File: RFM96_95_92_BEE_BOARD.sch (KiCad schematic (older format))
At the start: 3 parts

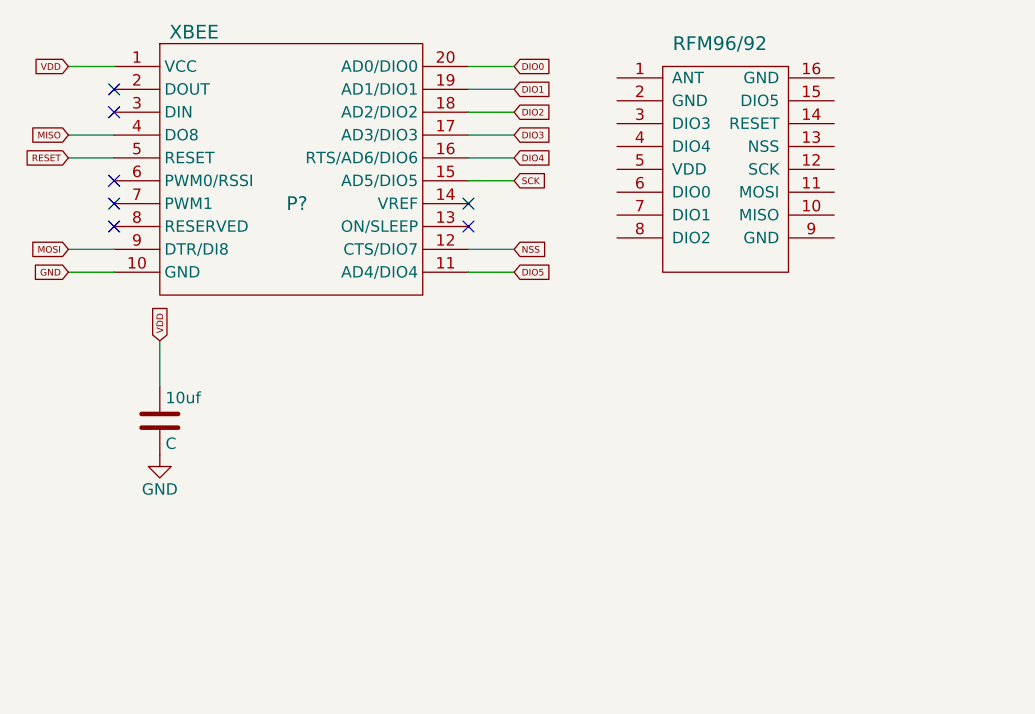
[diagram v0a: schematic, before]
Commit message: created library files and changed schematic
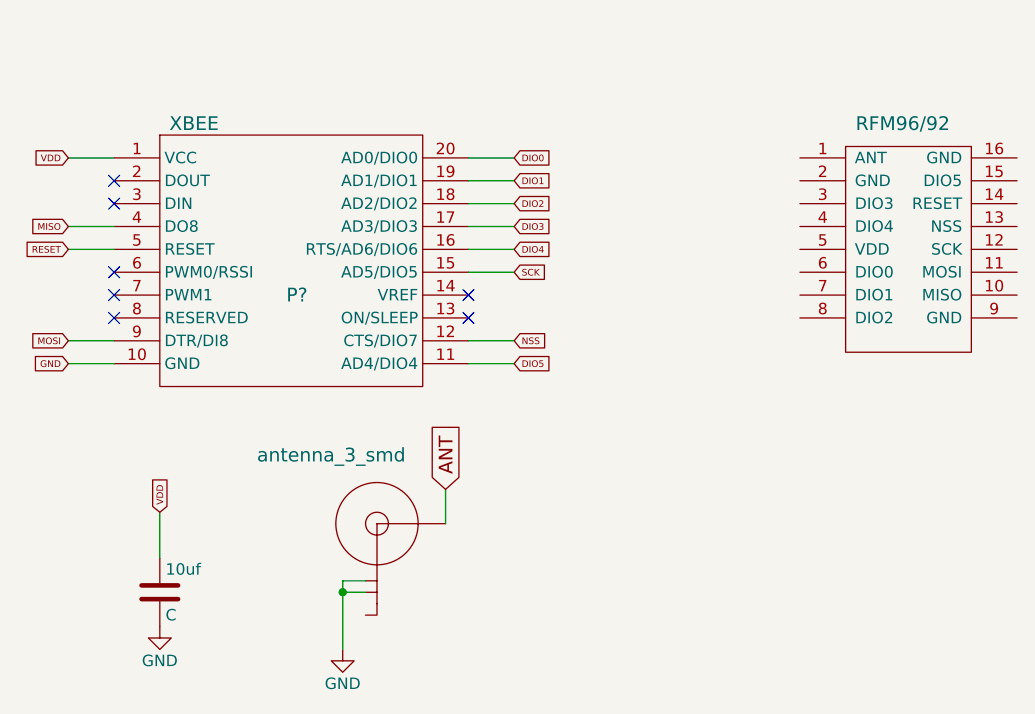
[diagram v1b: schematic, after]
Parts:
- added U?: antenna_3_smd, symbol antenna_3_smd
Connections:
- net labels added: ANT
- wire segments 14 -> 18
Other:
- moved on the sheet: 10uf, P?
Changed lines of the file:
@@
 LIBS:valves
 LIBS:RFM96_95_92
-LIBS:conn_8_16
-LIBS:conn_08_16
+LIBS:xbee
 LIBS:antenna
 LIBS:antenna_3_smd
-LIBS:conn_8_16_1
-LIBS:xbee
 LIBS:RFM96_95_92_BEE_BOARD-cache
 EELAYER 25 0
@@
 L RFM96/92 U?
 U 1 1 58359992
-P 5550 1600
-F 0 "U?" H 5600 1000 60  0001 C CNN
-F 1 "RFM96/92" H 5550 2150 60  0000 C CNN
-F 2 "" H 5750 1800 60  0001 C CNN
-F 3 "" H 5750 1800 60  0001 C CNN
-	1    5550 1600
+P 6350 1950
+F 0 "U?" H 6400 1350 60  0001 C CNN
+F 1 "RFM96/92" H 6350 2500 60  0000 C CNN
+F 2 "" H 6550 2150 60  0001 C CNN
+F 3 "" H 6550 2150 60  0001 C CNN
+	1    6350 1950
 	1    0    0    -1
 $EndComp
@@
 L XBEE P?
 U 1 1 583689AA
-P 3650 1700
-F 0 "P?" H 3700 1650 60  0000 C CNN
-F 1 "XBEE" H 3250 2400 60  0000 C CNN
-F 2 "" H 3650 1700 60  0001 C CNN
-F 3 "" H 3650 1700 60  0001 C CNN
-	1    3650 1700
+P 3650 2100
+F 0 "P?" H 3700 2050 60  0000 C CNN
+F 1 "XBEE" H 3250 2800 60  0000 C CNN
+F 2 "" H 3650 2100 60  0001 C CNN
+F 3 "" H 3650 2100 60  0001 C CNN
+	1    3650 2100
 	1    0    0    -1
 $EndComp
-NoConn ~ 4450 1750
-Text GLabel 2700 1150 0    29   Input ~ 0
+NoConn ~ 4450 2150
+Text GLabel 2700 1550 0    29   Input ~ 0
 VDD
-NoConn ~ 2900 1250
-NoConn ~ 2900 1350
-Text GLabel 2700 1450 0    29   Input ~ 0
-MISO
-Text GLabel 2700 1550 0    29   Input ~ 0
-RESET
 NoConn ~ 2900 1650
 NoConn ~ 2900 1750
-NoConn ~ 2900 1850
+Text GLabel 2700 1850 0    29   Input ~ 0
+MISO
 Text GLabel 2700 1950 0    29   Input ~ 0
+RESET
+NoConn ~ 2900 2050
+NoConn ~ 2900 2150
+NoConn ~ 2900 2250
+Text GLabel 2700 2350 0    29   Input ~ 0
 MOSI
+Wire Wire Line
+	2700 2350 2900 2350
 Wire Wire Line
 	2700 1950 2900 1950
 Wire Wire Line
+	2700 1850 2900 1850
+Wire Wire Line
 	2700 1550 2900 1550
-Wire Wire Line
-	2700 1450 2900 1450
-Wire Wire Line
-	2700 1150 2900 1150
-Text GLabel 2700 2050 0    29   Input ~ 0
+Text GLabel 2700 2450 0    29   Input ~ 0
 GND
 Wire Wire Line
-	2900 2050 2700 2050
-Text GLabel 4650 1150 2    29   Input ~ 0
+	2900 2450 2700 2450
+Text GLabel 4650 1550 2    29   Input ~ 0
 DIO0
-Text GLabel 4650 1250 2    29   Input ~ 0
+Text GLabel 4650 1650 2    29   Input ~ 0
 DIO1
-Text GLabel 4650 1350 2    29   Input ~ 0
+Text GLabel 4650 1750 2    29   Input ~ 0
 DIO2
-Text GLabel 4650 1450 2    29   Input ~ 0
+Text GLabel 4650 1850 2    29   Input ~ 0
 DIO3
-Text GLabel 4650 1550 2    29   Input ~ 0
+Text GLabel 4650 1950 2    29   Input ~ 0
 DIO4
-Text GLabel 4650 2050 2    29   Input ~ 0
+Text GLabel 4650 2450 2    29   Input ~ 0
 DIO5
-Wire Wire Line
-	4650 1150 4450 1150
-Wire Wire Line
-	4650 1250 4450 1250
-Wire Wire Line
-	4650 1350 4450 1350
-Wire Wire Line
-	4650 1450 4450 1450
 Wire Wire Line
 	4650 1550 4450 1550
 Wire Wire Line
 	4650 1650 4450 1650
-Text GLabel 4650 1650 2    29   Input ~ 0
-SCK
-Text GLabel 4650 1950 2    29   Input ~ 0
-NSS
+Wire Wire Line
+	4650 1750 4450 1750
+Wire Wire Line
+	4650 1850 4450 1850
 Wire Wire Line
 	4650 1950 4450 1950
 Wire Wire Line
 	4650 2050 4450 2050
-NoConn ~ 4450 1850
+Text GLabel 4650 2050 2    29   Input ~ 0
+SCK
+Text GLabel 4650 2350 2    29   Input ~ 0
+NSS
+Wire Wire Line
+	4650 2350 4450 2350
+Wire Wire Line
+	4650 2450 4450 2450
+NoConn ~ 4450 2250
 $Comp
 L C 10uf
 U 1 1 5836A82C
-P 3100 2700
-F 0 "10uf" H 3125 2800 50  0000 L CNN
-F 1 "C" H 3125 2600 50  0000 L CNN
-F 2 "" H 3138 2550 50  0000 C CNN
-F 3 "" H 3100 2700 50  0000 C CNN
-	1    3100 2700
+P 3100 3450
+F 0 "10uf" H 3125 3550 50  0000 L CNN
+F 1 "C" H 3125 3350 50  0000 L CNN
+F 2 "" H 3138 3300 50  0000 C CNN
+F 3 "" H 3100 3450 50  0000 C CNN
+	1    3100 3450
 	1    0    0    -1
 $EndComp
@@
 L GND #PWR?
 U 1 1 5836A8D1
-P 3100 2850
-F 0 "#PWR?" H 3100 2600 50  0001 C CNN
-F 1 "GND" H 3100 2700 50  0000 C CNN
-F 2 "" H 3100 2850 50  0000 C CNN
-F 3 "" H 3100 2850 50  0000 C CNN
-	1    3100 2850
+P 3100 3600
+F 0 "#PWR?" H 3100 3350 50  0001 C CNN
+F 1 "GND" H 3100 3450 50  0000 C CNN
+F 2 "" H 3100 3600 50  0000 C CNN
+F 3 "" H 3100 3600 50  0000 C CNN
+	1    3100 3600
 	1    0    0    -1
 $EndComp
 Wire Wire Line
-	3100 2350 3100 2550
-Text GLabel 3100 2350 1    29   Input ~ 0
+	3100 3100 3100 3300
+Text GLabel 3100 3100 1    29   Input ~ 0
 VDD
+Wire Wire Line
+	4000 3400 3900 3400
+Wire Wire Line
+	3900 3400 3900 3700
+Wire Wire Line
+	3900 3450 4000 3450
+Connection ~ 3900 3450
+$Comp
+L GND #PWR?
+U 1 1 5836B838
+P 3900 3700
+F 0 "#PWR?" H 3900 3450 50  0001 C CNN
+F 1 "GND" H 3900 3550 50  0000 C CNN
+F 2 "" H 3900 3700 50  0000 C CNN
+F 3 "" H 3900 3700 50  0000 C CNN
+	1    3900 3700
+	1    0    0    -1
+$EndComp
+$Comp
+L antenna_3_smd U?
+U 1 1 5836B792
+P 4050 3150
+F 0 "U?" H 4100 3500 60  0001 C CNN
+F 1 "antenna_3_smd" H 3850 3450 60  0000 C CNN
+F 2 "" H 4050 3150 60  0001 C CNN
+F 3 "" H 4050 3150 60  0001 C CNN
+	1    4050 3150
+	1    0    0    -1
+$EndComp
+Wire Wire Line
+	4350 3150 4350 3000
+Text GLabel 4350 3000 1    60   Input ~ 0
+ANT
 $EndSCHEMATC
